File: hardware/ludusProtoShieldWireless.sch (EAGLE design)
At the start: 72 parts, among them Q1 MOSFET-NCHANNELSMD, Q2 MOSFET-NCHANNELSMD, U1 ARDUINO, U3 TB6612FNG

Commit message: Updated shield footprint to include staggered / locking holes
* changed filenames to ludusProtoShieldWireless
* repo name will change after this commit
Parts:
- JP22: device SparkFun-Connectors:M04SMD_STRAIGHT_COMBO -> SparkFun-Connectors:M04LOCK
- U1: device SparkFun-Boards:ARDUINO_R3_SHIELDNOLABELS -> SparkFun-Boards:ARDUINO_R3_SHIELDUNO_R3_SHIELD_NOLABELS_LOCK
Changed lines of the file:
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@@
 <grid distance="0.1" unitdist="inch" unit="inch" style="lines" multiple="1" display="no" altdistance="0.01" altunitdist="inch" altunit="inch"/>
 <layers>
-<layer number="1" name="Top" color="4" fill="1" visible="no" active="no"/>
-<layer number="2" name="Route2" color="1" fill="3" visible="no" active="no"/>
-<layer number="3" name="Route3" color="4" fill="3" visible="no" active="no"/>
-<layer number="4" name="Route4" color="1" fill="4" visible="no" active="no"/>
-<layer number="5" name="Route5" color="4" fill="4" visible="no" active="no"/>
-<layer number="6" name="Route6" color="1" fill="8" visible="no" active="no"/>
-<layer number="7" name="Route7" color="4" fill="8" visible="no" active="no"/>
-<layer number="8" name="Route8" color="1" fill="2" visible="no" active="no"/>
-<layer number="9" name="Route9" color="4" fill="2" visible="no" active="no"/>
-<layer number="10" name="Route10" color="1" fill="7" visible="no" active="no"/>
-<layer number="11" name="Route11" color="4" fill="7" visible="no" active="no"/>
-<layer number="12" name="Route12" color="1" fill="5" visible="no" active="no"/>
-<layer number="13" name="Route13" color="4" fill="5" visible="no" active="no"/>
-<layer number="14" name="Route14" color="1" fill="6" visible="no" active="no"/>
-<layer number="15" name="Route15" color="4" fill="6" visible="no" active="no"/>
-<layer number="16" name="Bottom" color="1" fill="1" visible="no" active="no"/>
-<layer number="17" name="Pads" color="2" fill="1" visible="no" active="no"/>
-<layer number="18" name="Vias" color="2" fill="1" visible="no" active="no"/>
-<layer number="19" name="Unrouted" color="6" fill="1" visible="no" active="no"/>
-<layer number="20" name="Dimension" color="15" fill="1" visible="no" active="no"/>
-<layer number="21" name="tPlace" color="16" fill="1" visible="no" active="no"/>
-<layer number="22" name="bPlace" color="14" fill="1" visible="no" active="no"/>
-<layer number="23" name="tOrigins" color="15" fill="1" visible="no" active="no"/>
-<layer number="24" name="bOrigins" color="15" fill="1" visible="no" active="no"/>
-<layer number="25" name="tNames" color="7" fill="1" visible="no" active="no"/>
-<layer number="26" name="bNames" color="7" fill="1" visible="no" active="no"/>
-<layer number="27" name="tValues" color="7" fill="1" visible="no" active="no"/>
-<layer number="28" name="bValues" color="7" fill="1" visible="no" active="no"/>
+<layer number="1" name="Top" color="4" fill="1" visible="yes" active="no"/>
+<layer number="2" name="Route2" color="1" fill="3" visible="yes" active="no"/>
+<layer number="3" name="Route3" color="4" fill="3" visible="yes" active="no"/>
+<layer number="4" name="Route4" color="1" fill="4" visible="yes" active="no"/>
+<layer number="5" name="Route5" color="4" fill="4" visible="yes" active="no"/>
+<layer number="6" name="Route6" color="1" fill="8" visible="yes" active="no"/>
+<layer number="7" name="Route7" color="4" fill="8" visible="yes" active="no"/>
+<layer number="8" name="Route8" color="1" fill="2" visible="yes" active="no"/>
+<layer number="9" name="Route9" color="4" fill="2" visible="yes" active="no"/>
+<layer number="10" name="Route10" color="1" fill="7" visible="yes" active="no"/>
+<layer number="11" name="Route11" color="4" fill="7" visible="yes" active="no"/>
+<layer number="12" name="Route12" color="1" fill="5" visible="yes" active="no"/>
+<layer number="13" name="Route13" color="4" fill="5" visible="yes" active="no"/>
+<layer number="14" name="Route14" color="1" fill="6" visible="yes" active="no"/>
+<layer number="15" name="Route15" color="4" fill="6" visible="yes" active="no"/>
+<layer number="16" name="Bottom" color="1" fill="1" visible="yes" active="no"/>
+<layer number="17" name="Pads" color="2" fill="1" visible="yes" active="no"/>
+<layer number="18" name="Vias" color="2" fill="1" visible="yes" active="no"/>
+<layer number="19" name="Unrouted" color="6" fill="1" visible="yes" active="no"/>
+<layer number="20" name="Dimension" color="15" fill="1" visible="yes" active="no"/>
+<layer number="21" name="tPlace" color="16" fill="1" visible="yes" active="no"/>
+<layer number="22" name="bPlace" color="14" fill="1" visible="yes" active="no"/>
+<layer number="23" name="tOrigins" color="15" fill="1" visible="yes" active="no"/>
+<layer number="24" name="bOrigins" color="15" fill="1" visible="yes" active="no"/>
+<layer number="25" name="tNames" color="7" fill="1" visible="yes" active="no"/>
+<layer number="26" name="bNames" color="7" fill="1" visible="yes" active="no"/>
+<layer number="27" name="tValues" color="7" fill="1" visible="yes" active="no"/>
+<layer number="28" name="bValues" color="7" fill="1" visible="yes" active="no"/>
 <layer number="29" name="tStop" color="7" fill="3" visible="no" active="no"/>
 <layer number="30" name="bStop" color="7" fill="6" visible="no" active="no"/>
@@
 <layer number="35" name="tGlue" color="7" fill="4" visible="no" active="no"/>
 <layer number="36" name="bGlue" color="7" fill="5" visible="no" active="no"/>
-<layer number="37" name="tTest" color="7" fill="1" visible="no" active="no"/>
-<layer number="38" name="bTest" color="7" fill="1" visible="no" active="no"/>
+<layer number="37" name="tTest" color="7" fill="1" visible="yes" active="no"/>
+<layer number="38" name="bTest" color="7" fill="1" visible="yes" active="no"/>
 <layer number="39" name="tKeepout" color="4" fill="11" visible="no" active="no"/>
 <layer number="40" name="bKeepout" color="1" fill="11" visible="no" active="no"/>
@@
 <layer number="44" name="Drills" color="7" fill="1" visible="no" active="no"/>
 <layer number="45" name="Holes" color="7" fill="1" visible="no" active="no"/>
-<layer number="46" name="Milling" color="3" fill="1" visible="no" active="no"/>
-<layer number="47" name="Measures" color="7" fill="1" visible="no" active="no"/>
-<layer number="48" name="Document" color="7" fill="1" visible="no" active="no"/>
-<layer number="49" name="Reference" color="7" fill="1" visible="no" active="no"/>
-<layer number="50" name="dxf" color="7" fill="1" visible="no" active="no"/>
-<layer number="51" name="tDocu" color="6" fill="1" visible="no" active="no"/>
-<layer number="52" name="bDocu" color="7" fill="1" visible="no" active="no"/>
-<layer number="53" name="tGND_GNDA" color="7" fill="9" visible="no" active="no"/>
-<layer number="54" name="bGND_GNDA" color="1" fill="9" visible="no" active="no"/>
-<layer number="56" name="wert" color="7" fill="1" visible="no" active="no"/>
-<layer number="57" name="tCAD" color="7" fill="1" visible="no" active="no"/>
+<layer number="46" name="Milling" color="3" fill="1" visible="yes" active="no"/>
+<layer number="47" name="Measures" color="7" fill="1" visible="yes" active="no"/>
+<layer number="48" name="Document" color="7" fill="1" visible="yes" active="no"/>
+<layer number="49" name="Reference" color="7" fill="1" visible="yes" active="no"/>
+<layer number="50" name="dxf" color="7" fill="1" visible="yes" active="no"/>
+<layer number="51" name="tDocu" color="6" fill="1" visible="yes" active="no"/>
+<layer number="52" name="bDocu" color="7" fill="1" visible="yes" active="no"/>
+<layer number="53" name="tGND_GNDA" color="7" fill="9" visible="yes" active="no"/>
+<layer number="54" name="bGND_GNDA" color="1" fill="9" visible="yes" active="no"/>
+<layer number="56" name="wert" color="7" fill="1" visible="yes" active="no"/>
+<layer number="57" name="tCAD" color="7" fill="1" visible="yes" active="no"/>
 <layer number="90" name="Modules" color="5" fill="1" visible="yes" active="yes"/>
 <layer number="91" name="Nets" color="2" fill="1" visible="yes" active="yes"/>
@@
 <part name="LED3" library="SparkFun-LED" deviceset="LED" device="0603" value="Blue"/>
 <part name="LED4" library="SparkFun-LED" deviceset="LED" device="0603" value="Blue"/>
-<part name="U1" library="SparkFun-Boards" deviceset="ARDUINO_R3_SHIELD" device="NOLABELS" value="ARDUINO"/>
+<part name="U1" library="SparkFun-Boards" deviceset="ARDUINO_R3_SHIELD" device="UNO_R3_SHIELD_NOLABELS_LOCK" value="ARDUINO"/>
 <part name="GND13" library="SparkFun" deviceset="GND" device=""/>
 <part name="JP0" library="SparkFun-Connectors" deviceset="M03" device="LOCK" value="D0"/>
@@
 <part name="LOGO3" library="SparkFun-Aesthetics" deviceset="SFE_LOGO_FLAME" device=".2COP"/>
 <part name="LOGO4" library="SparkFun-Aesthetics" deviceset="SFE_LOGO_NAME_FLAME" device=".1_INCH" value="SFE_LOGO_NAME_FLAME.1_INCH"/>
-<part name="JP22" library="SparkFun-Connectors" deviceset="M04" device="SMD_STRAIGHT_COMBO"/>
+<part name="JP22" library="SparkFun-Connectors" deviceset="M04" device="LOCK"/>
 <part name="LED7" library="SparkFun-LED" deviceset="LED-RED" device="0603" value="Red"/>
 <part name="LED8" library="SparkFun-LED" deviceset="LED-GREEN" device="0603" value="Green"/>

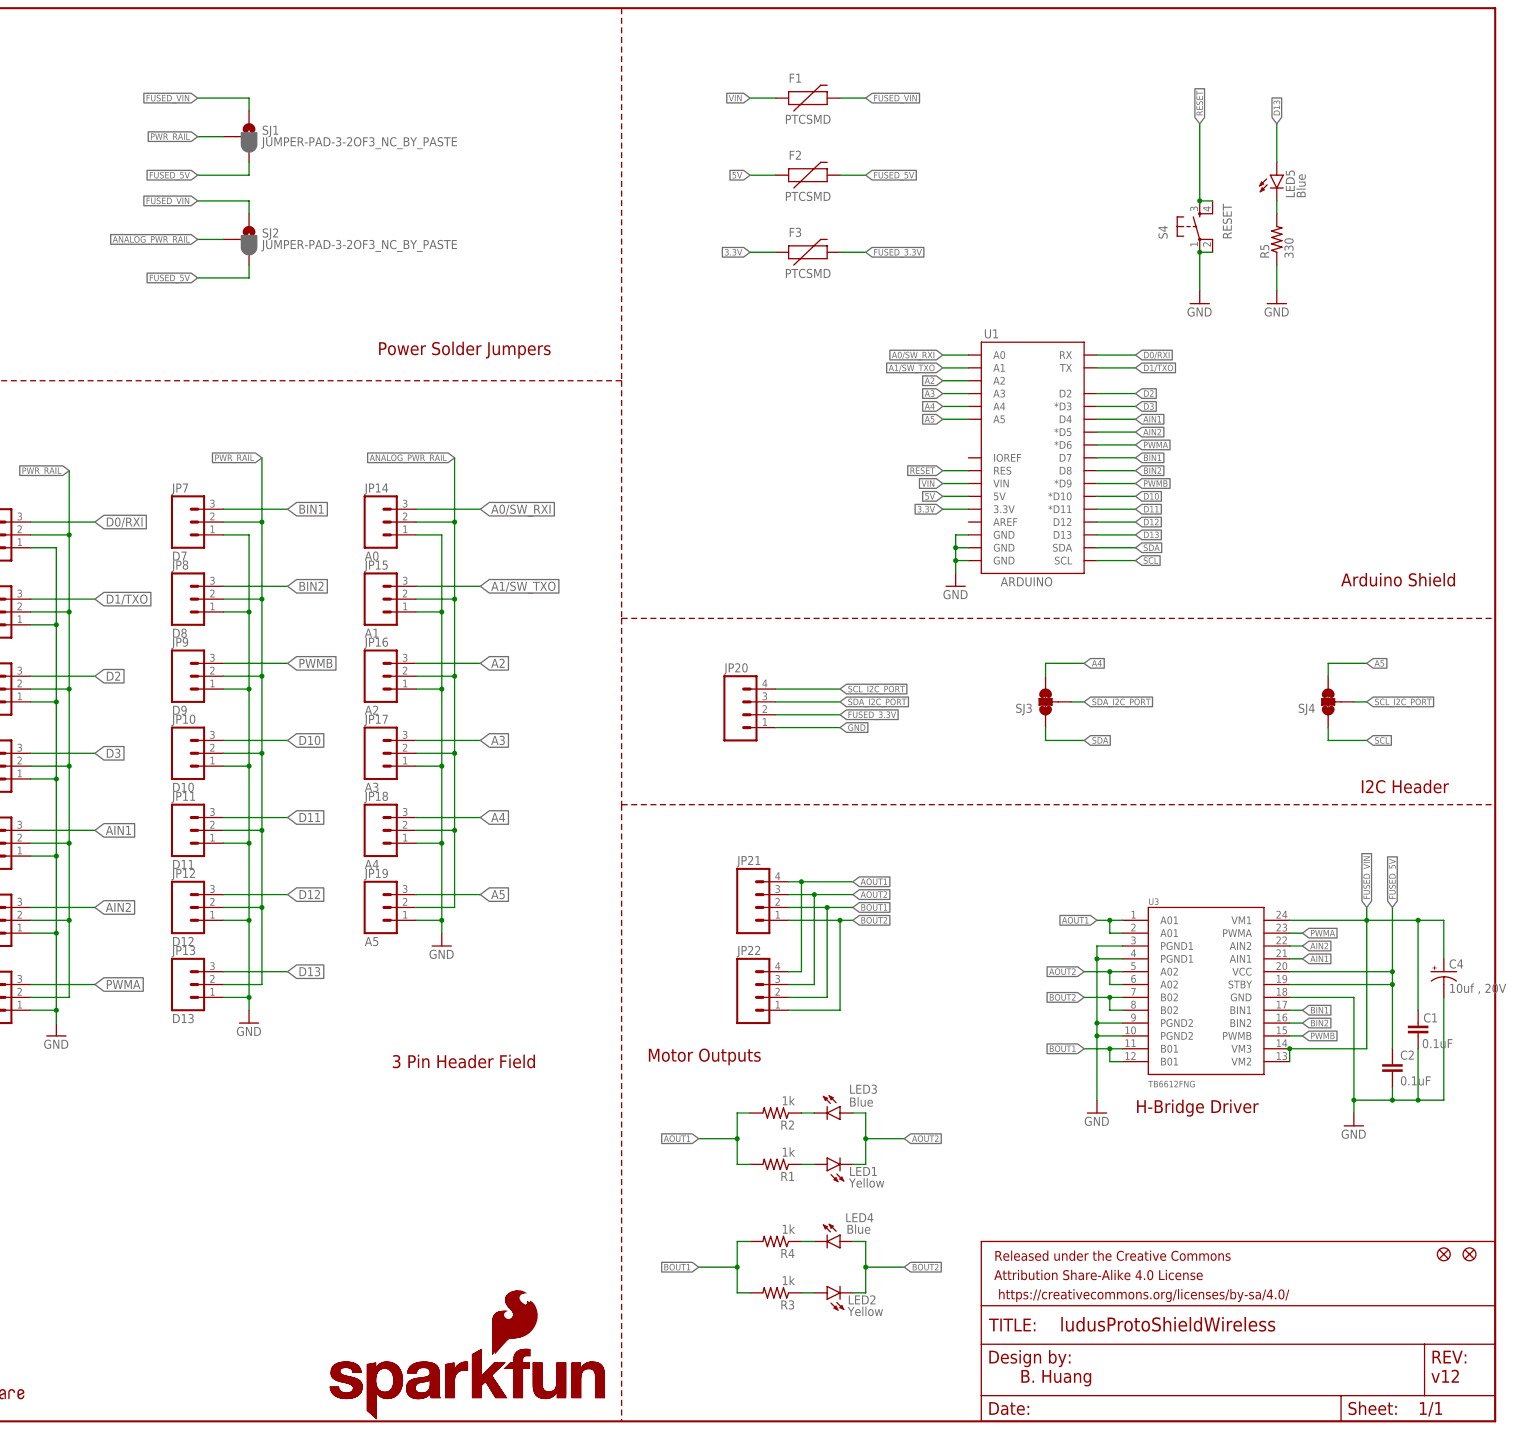
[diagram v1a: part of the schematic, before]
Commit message: Updated to fix all issues -
Also added a switch to shield for switching between VIN and 5V
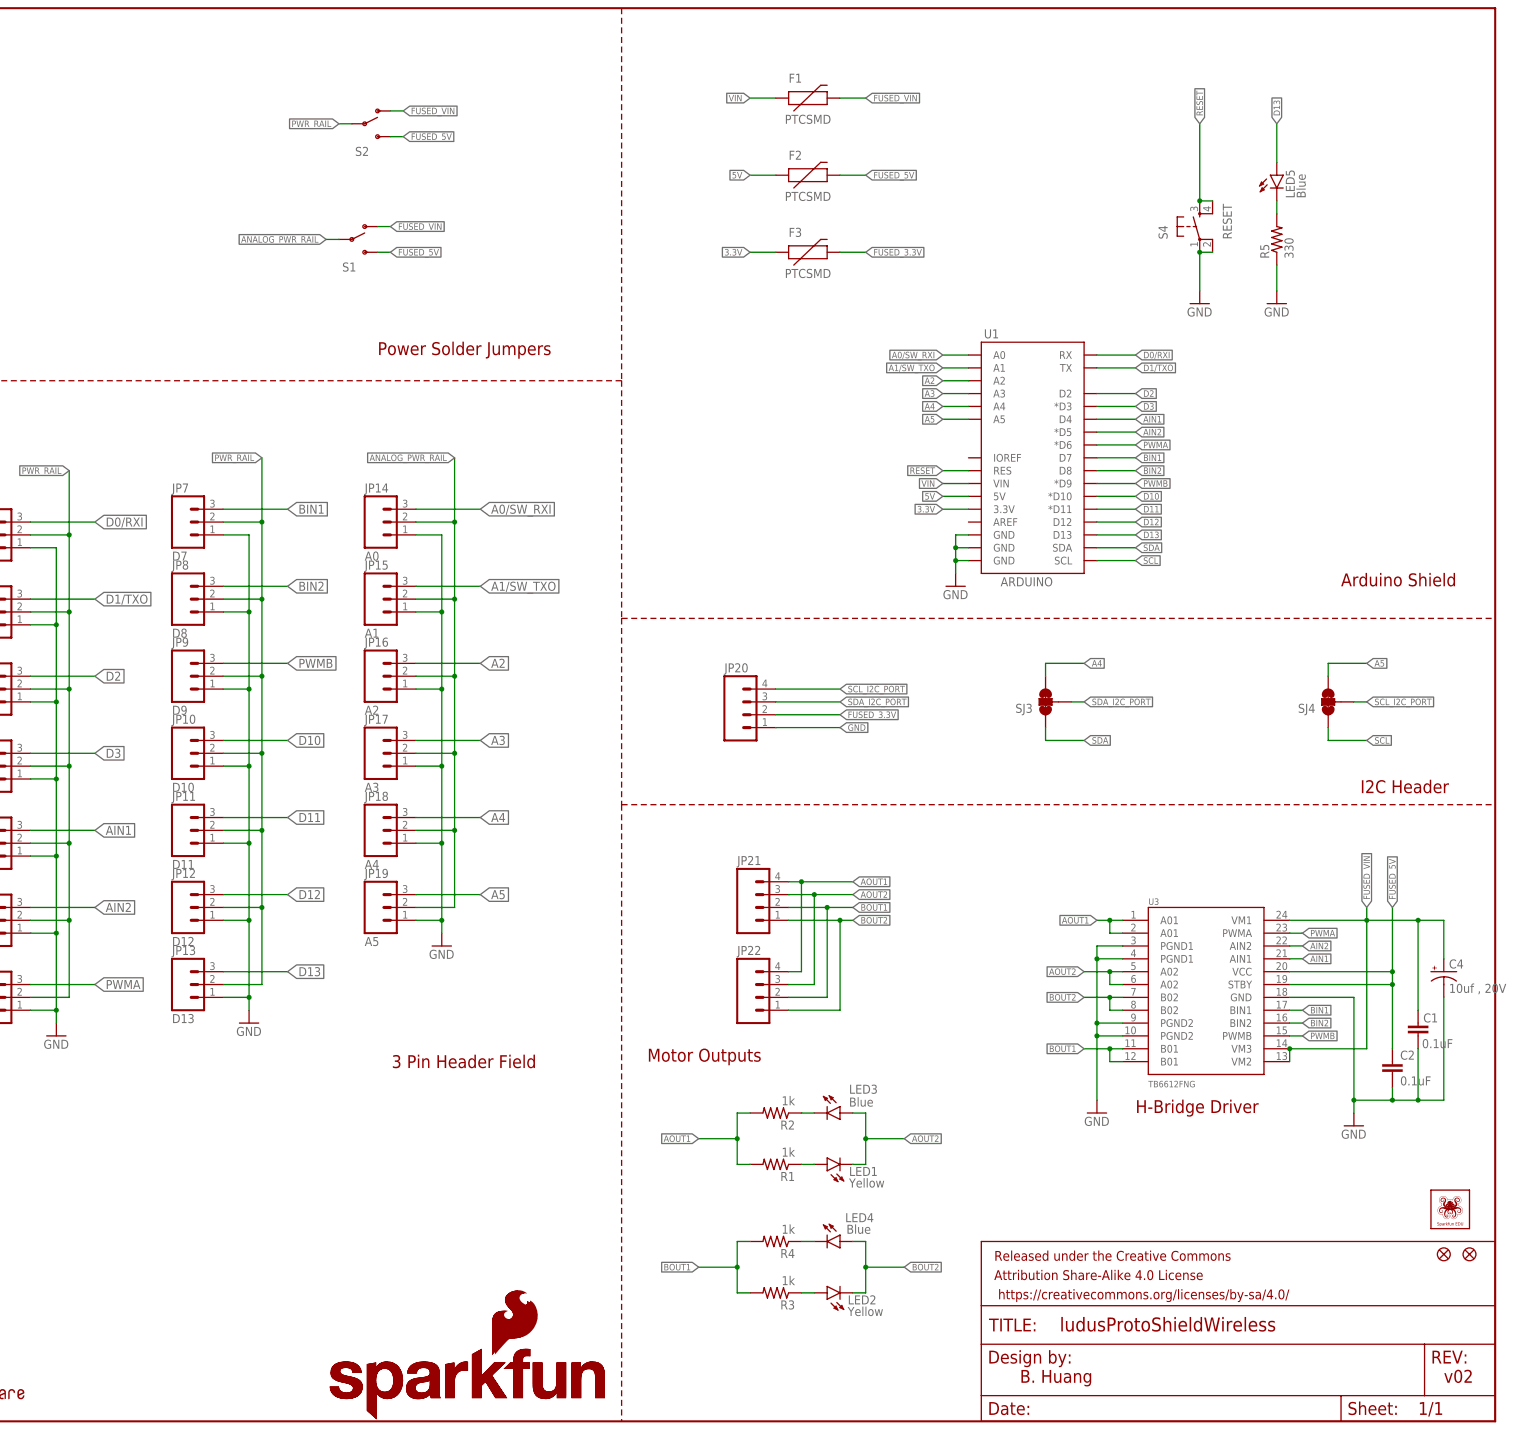
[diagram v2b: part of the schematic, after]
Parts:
- removed SJ1, SJ2: JUMPER-PAD-3-2OF3_NC_BY_PASTE, SparkFun-Passives:JUMPER-PAD-3-2OF3_NC_BY_PASTE
- added S1, S2: (no value), SparkFun-Electromechanical:SWITCH-SPDTSMD
- Q1, Q2: value MOSFET-NCHANNELSMD -> MOSFET-NCHANNELBSS138; device SparkFun-DiscreteSemi:MOSFET-NCHANNELSMD -> SparkFun-DiscreteSemi:MOSFET-NCHANNELBSS138
- U$1: value SFE_LUDUS -> SFE_LUDUSSFE_LUDUS-M; device SparkFun-Aesthetics:SFE_LUDUS -> SparkFun-Aesthetics:SFE_LUDUSSFE_LUDUS-M
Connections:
- net ANALOG_PWR_RAIL: now also S1.P; no longer SJ2.2
- net FUSED_5V: now also S1.S, S2.S; no longer SJ1.3, SJ2.3
- net FUSED_VIN: now also S1.O, S2.O; no longer SJ1.1, SJ2.1
- net PWR_RAIL: now also S2.P; no longer SJ1.2
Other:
- note added: "v02"
- note removed: "v12"
